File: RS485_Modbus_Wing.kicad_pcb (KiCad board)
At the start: 2 copper layers, 50.8 x 22.9 mm, 19 parts, among them J1 feather long, J2 feather short, J3 Screw_Terminal_01x02, U1 SP3485EN

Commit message: Labels
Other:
- board text added: "DE"
- board text added: "DI"
- board text added: "RE"
- board text added: "RO"
- board text removed: "D10"
- board text removed: "D11"
- board text removed: "D12"
- board text removed: "D9"
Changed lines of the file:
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@@
     (effects (font (size 0.7 0.7) (thickness 0.125)))
   )
-  (gr_text D12 (at 149.92 77.345) (layer F.SilkS)
+  (gr_text DI (at 149.92 77.345) (layer F.SilkS)
     (effects (font (size 0.7 0.7) (thickness 0.125)))
   )
-  (gr_text D11 (at 152.46 77.345) (layer F.SilkS)
+  (gr_text DE (at 152.46 77.345) (layer F.SilkS)
     (effects (font (size 0.7 0.7) (thickness 0.125)))
   )
-  (gr_text D10 (at 155 77.345) (layer F.SilkS)
+  (gr_text RE (at 155 77.345) (layer F.SilkS)
     (effects (font (size 0.7 0.7) (thickness 0.125)))
   )
-  (gr_text D9 (at 157.54 77.345) (layer F.SilkS)
+  (gr_text RO (at 157.54 77.345) (layer F.SilkS)
     (effects (font (size 0.7 0.7) (thickness 0.125)))
   )

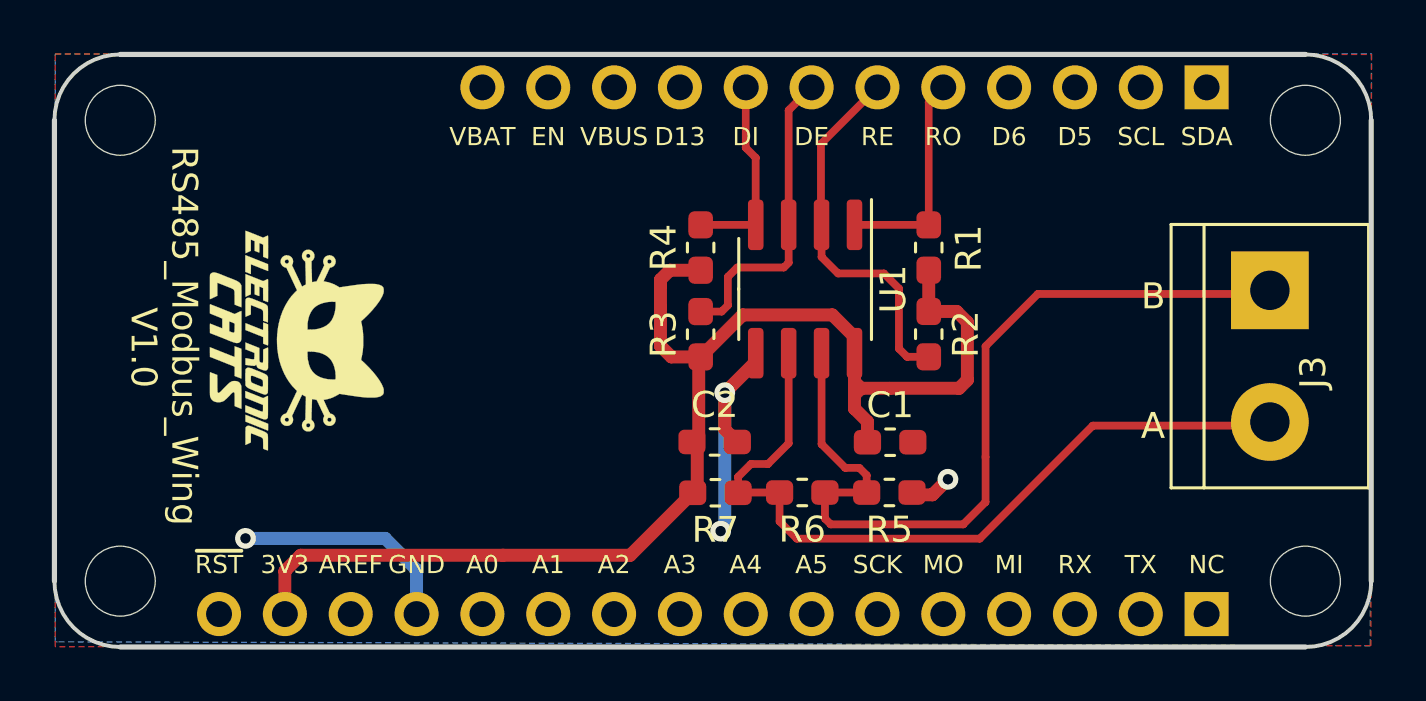
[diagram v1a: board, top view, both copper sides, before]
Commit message: fix labels and logos
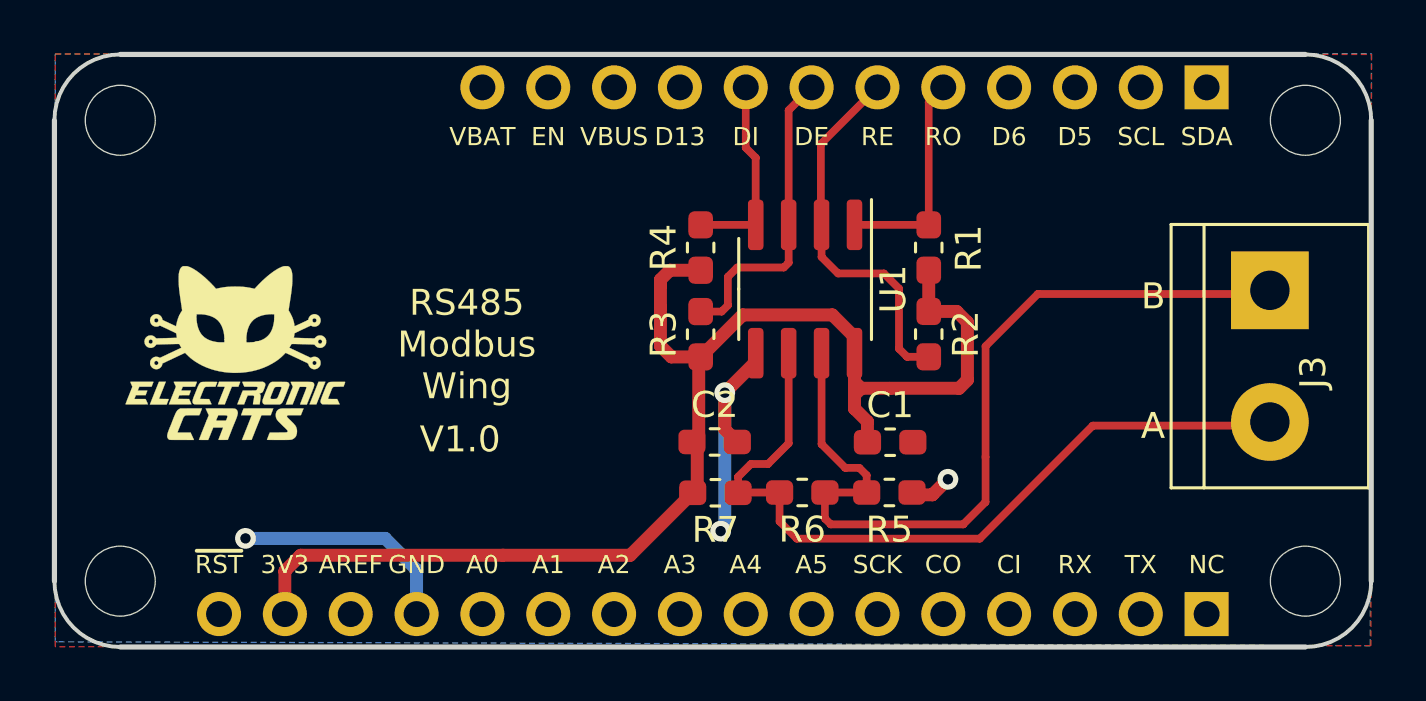
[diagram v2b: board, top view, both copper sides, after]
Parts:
- removed the G*** at (131.2, 85.0)
- added G***: LOGO, Aesthetics:electronic_cats_logo_8x6, B.Cu at (157.0, 84.7)
- added REF**: OSHW-Logo_7.5x8mm_SilkScreen, Symbol:OSHW-Logo_7.5x8mm_SilkScreen, B.Cu at (140.8, 85.0)
- moved G*** 2.42 mm to (130.2, 85.7), turned to 0 degrees
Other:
- board text added: "CI"
- board text added: "CO"
- board text added: "RS485 Modbus Wing"
- board text removed: "MI"
- board text removed: "MO"
- board text removed: "RS485_Modbus_Wing"

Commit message: Change_conection
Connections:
- J1 pad 2: /TX -> /DI
- J1 pad 3: /RX -> /RO
- J2 pad 5: /RO -> /D9
- J2 pad 8: /DI -> /D12
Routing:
- net /DI: track 7.59 -> 36.2 mm
- net /RO: track 8.40 -> 22.2 mm, vias 0 -> 1
- net GND: track 19.9 -> 14.3 mm
- net /RS485B: track 33.4 -> 31.9 mm
- net /RS485A: track 30.2 -> 29.6 mm
- net +3V3: track 52.9 -> 52.7 mm, vias 0 -> 1
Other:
- board text added: "D12"
- board text added: "D9"
- board text removed: "DI"
- board text removed: "RO"

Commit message: Change_labels
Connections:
- net /DI renamed /TX
- net /RO renamed /RX
